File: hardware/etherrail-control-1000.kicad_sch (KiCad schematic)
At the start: 33 parts, among them J1 Conn_02x04_Odd_Even, J2 Conn_01x04, U1 AMS1117-3.3, U2 ESP32-C3, Y2 Crystal_GND24

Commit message: Fix missing crystal speed property
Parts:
- Y2: value Crystal_GND24 -> 16.000MHz GND24
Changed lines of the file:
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@@
       (effects (font (size 1.27 1.27)))
     )
-    (property "Value" "Crystal_GND24" (at 125.73 112.6491 0)
+    (property "Value" " 16.000MHz GND24" (at 125.73 112.6491 0)
       (effects (font (size 1.27 1.27)))
     )

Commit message: WIP: Add revised hardware
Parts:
- removed D5: D, Diode_SMD:D_SOD-323, symbol Device:D
- removed D8: Yellow, LED_SMD:LED_0603_1608Metric, symbol Device:LED
- added 3VR1: ME6118, Package_TO_SOT_SMD:SOT-89-3, symbol Regulator_Linear:AMS1117-3.3
- added C14: 1mF 6.3V, Capacitor_Tantalum_SMD:CP_EIA-7343-43_Kemet-X, symbol Device:C
- added D5: Yellow, LED_SMD:LED_0603_1608Metric, symbol Device:LED
- added JP1, JP2: Jumper_2_Open, Jumper:SolderJumper-2_P1.3mm_Open_Pad1.0x1.5mm, symbol Jumper:Jumper_2_Open
- added Q1, Q2: AO3400A, Package_TO_SOT_SMD:SOT-23, symbol Transistor_FET:AO3400A
- added R5: 100k, Resistor_SMD:R_0402_1005Metric, symbol Device:R
- added R6: 10k, Resistor_SMD:R_0201_0603Metric, symbol Device:R
- added R7: 22, Resistor_SMD:R_0201_0603Metric, symbol Device:R
- added R8: 5.1k, Resistor_SMD:R_0201_0603Metric, symbol Device:R
- 6VR1: renamed from U1; value AMS1117-3.3 -> 78N06G; LCSC (none) -> C84863
- C1: value 100uF -> 1mF 6.3V; footprint Capacitor_Tantalum_SMD:CP_EIA-7343-30_AVX-N -> Capacitor_Tantalum_SMD:CP_EIA-7343-43_Kemet-X; LCSC (none) -> C696799
- D7: LCSC (none) -> C19171392
- J2: footprint Connector_PinHeader_1.00mm:PinHeader_1x04_P1.00mm_Vertical -> Connector_PinHeader_1.27mm:PinHeader_1x04_P1.27mm_Vertical
- U2: LCSC (none) -> C2838500
- U3: LCSC (none) -> C2832995
- Y2: value 16.000MHz GND24 -> 40.000MHz 15pF; LCSC Part (none) -> C9010
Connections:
- net USB Power In is gone; now on net Light Common (+): J2.1 (Pin_1)
- net Unfiltered Power In is gone; now on net Light Common (+): D1.1 (K), D4.1 (K), D6.2 (A), R1.1, U3.4 (VDD)
- net Controller Power: now also 3VR1.2 (VO), R6.2, R8.1; no longer 6VR1.2 (VO)
- net GND: now also 3VR1.1 (GND), C14.2, D5.1 (K), JP1.2 (B), JP2.2 (B), Q1.2 (S), Q2.2 (S), R5.2
- net Light Front (-): now also Q1.3 (D)
- net Light Rear (-): now also Q2.3 (D)
- net Motor Controlling Direction: now also U2.24 (SPIQ/GPIO17); no longer U2.23 (SPID/GPIO16)
- net Motor Controlling PWM: now also U2.23 (SPID/GPIO16); no longer U2.24 (SPIQ/GPIO17)
- net USB Data Negative: now also J2.2 (Pin_2); no longer J2.3 (Pin_3)
- net USB Data Positive: now also J2.3 (Pin_3); no longer J2.2 (Pin_2)
- net at 6VR1.3 (VI), D6.1 (K): no longer C1.1
- net at C9.1, Y2.3: now also R7.1; no longer U2.30 (XTAL_P)
- net at R4.2: now also D5.2 (A)
- net at R4.1: now also U2.16 (GPIO10); no longer U2.14 (GPIO8)
- net Bootmode: now reaches U2.15 (GPIO9/BOOT)
- net Bootmode: now also JP1.1 (A), R8.2
- net Logic Level Light Front: now reaches U2.21 (SPICS0/GPIO14)
- net Logic Level Light Front: now also Q1.1 (G)
- net Logic Level Light Rear: now reaches U2.22 (SPICLK/GPIO15)
- net Logic Level Light Rear: now also Q2.1 (G)
- new net: 3VR1.3 (VI), 6VR1.2 (VO), C1.1, C14.1, R5.1
- new net: R7.2, U2.30 (XTAL_P)
- new net Download Enable: JP2.1 (A), R6.1, U2.14 (GPIO8)
- no-connect marks 19 -> 15
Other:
- moved on the sheet: 6VR1, C11, D7, J1, R1, R2, R3

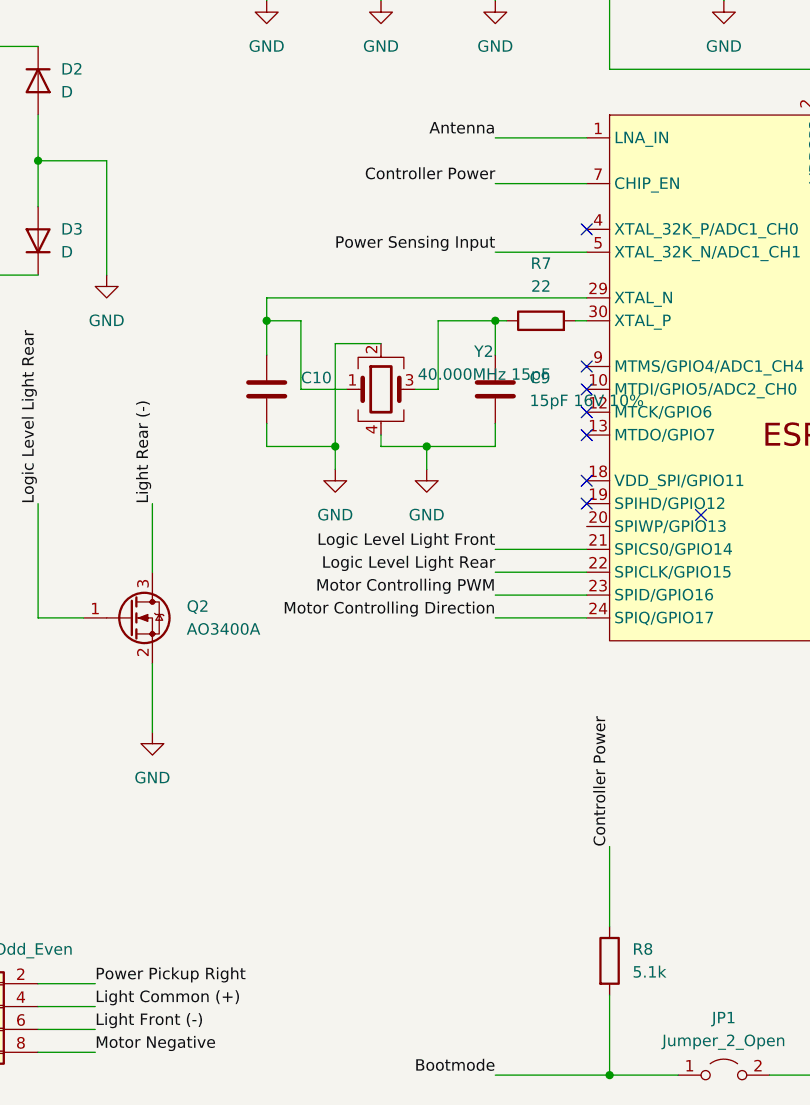
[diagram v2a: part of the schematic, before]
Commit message: Add EN jumper
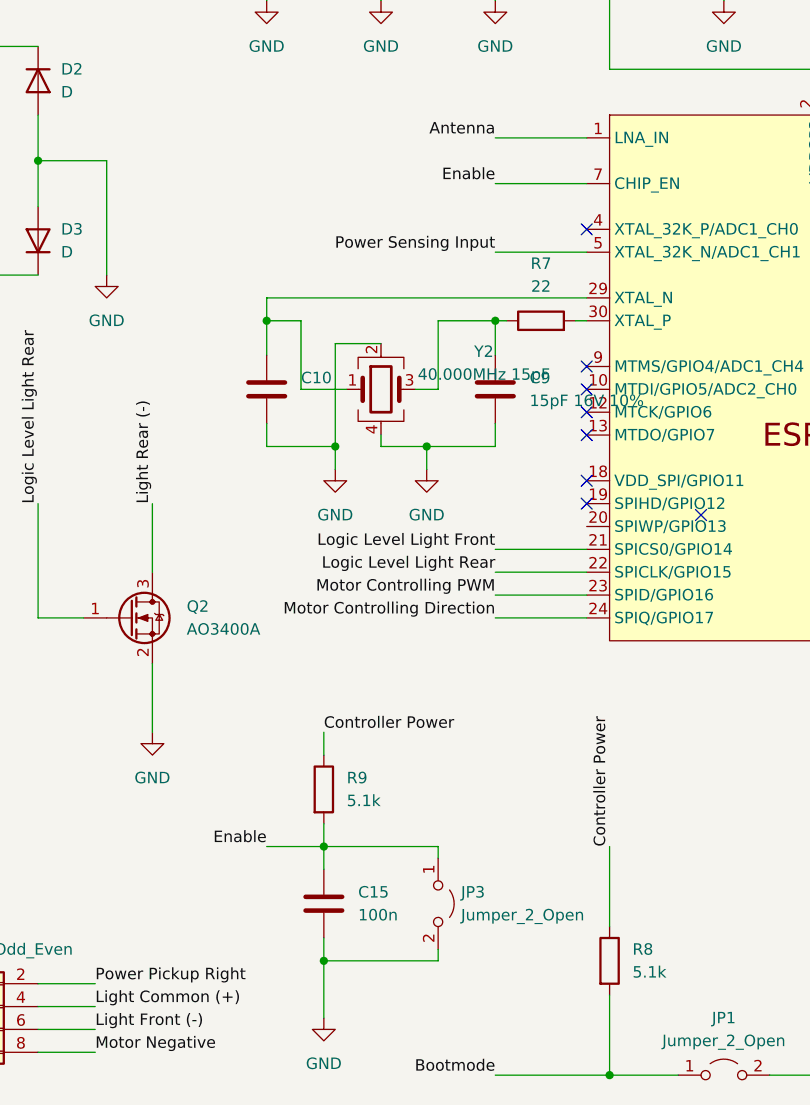
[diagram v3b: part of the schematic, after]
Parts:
- added C15: 100n, Capacitor_SMD:C_0201_0603Metric, symbol Device:C
- added JP3: Jumper_2_Open, Jumper:SolderJumper-2_P1.3mm_Open_Pad1.0x1.5mm, symbol Jumper:Jumper_2_Open
- added R9: 5.1k, Resistor_SMD:R_0201_0603Metric, symbol Device:R
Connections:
- net Controller Power: now also R9.1; no longer U2.7 (CHIP_EN)
- net GND: now also C15.2, JP3.2 (B)
- new net Enable: C15.1, JP3.1 (A), R9.2, U2.7 (CHIP_EN)
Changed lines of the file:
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@@
   (junction (at 127 106.68) (diameter 0) (color 0 0 0 0)
   )
+  (junction (at 107.95 165.1) (diameter 0) (color 0 0 0 0)
+  )
   (junction (at 203.2 57.15) (diameter 0) (color 0 0 0 0)
   )
@@
   )
   (junction (at 76.2 25.4) (diameter 0) (color 0 0 0 0)
+  )
+  (junction (at 107.95 177.8) (diameter 0) (color 0 0 0 0)
   )
   (junction (at 157.48 57.15) (diameter 0) (color 0 0 0 0)
@@
     (stroke (width 0) (type default))
   )
+  (wire (pts (xy 107.95 184.15) (xy 107.95 177.8))
+    (stroke (width 0) (type default))
+  )
   (wire (pts (xy 31.75 166.37) (xy 31.75 168.91))
     (stroke (width 0) (type default))
@@
     (stroke (width 0) (type default))
   )
+  (wire (pts (xy 107.95 165.1) (xy 107.95 162.56))
+    (stroke (width 0) (type default))
+  )
   (wire (pts (xy 57.15 187.96) (xy 63.5 187.96))
     (stroke (width 0) (type default))
@@
     (stroke (width 0) (type default))
   )
+  (wire (pts (xy 120.65 165.1) (xy 107.95 165.1))
+    (stroke (width 0) (type default))
+  )
   (wire (pts (xy 127 67.31) (xy 127 71.12))
     (stroke (width 0) (type default))
@@
     (stroke (width 0) (type default))
   )
+  (wire (pts (xy 107.95 165.1) (xy 107.95 167.64))
+    (stroke (width 0) (type default))
+  )
   (wire (pts (xy 88.9 25.4) (xy 88.9 34.29))
     (stroke (width 0) (type default))
@@
     (stroke (width 0) (type default))
   )
+  (wire (pts (xy 120.65 166.37) (xy 120.65 165.1))
+    (stroke (width 0) (type default))
+  )
   (wire (pts (xy 254 147.32) (xy 254 152.4))
     (stroke (width 0) (type default))
@@
     (stroke (width 0) (type default))
   )
+  (wire (pts (xy 107.95 177.8) (xy 120.65 177.8))
+    (stroke (width 0) (type default))
+  )
   (wire (pts (xy 38.1 38.1) (xy 38.1 25.4))
     (stroke (width 0) (type default))
@@
     (stroke (width 0) (type default))
   )
+  (wire (pts (xy 101.6 165.1) (xy 107.95 165.1))
+    (stroke (width 0) (type default))
+  )
   (wire (pts (xy 101.6 57.15) (xy 101.6 59.69))
     (stroke (width 0) (type default))
@@
     (stroke (width 0) (type default))
   )
+  (wire (pts (xy 107.95 152.4) (xy 107.95 154.94))
+    (stroke (width 0) (type default))
+  )
+  (wire (pts (xy 107.95 175.26) (xy 107.95 177.8))
+    (stroke (width 0) (type default))
+  )
   (wire (pts (xy 152.4 57.15) (xy 157.48 57.15))
     (stroke (width 0) (type default))
@@
     (stroke (width 0) (type default))
   )
+  (wire (pts (xy 120.65 176.53) (xy 120.65 177.8))
+    (stroke (width 0) (type default))
+  )
   (wire (pts (xy 237.49 44.45) (xy 228.6 44.45))
     (stroke (width 0) (type default))
@@
     (effects (font (size 1.27 1.27)) (justify right bottom))
   )
-  (label "Controller Power" (at 127 91.44 180) (fields_autoplaced)
-    (effects (font (size 1.27 1.27)) (justify right bottom))
-  )
   (label "Unfiltered Power In" (at 50.8 91.44 180) (fields_autoplaced)
     (effects (font (size 1.27 1.27)) (justify right bottom))
@@
     (effects (font (size 1.27 1.27)) (justify left bottom))
   )
+  (label "Enable" (at 101.6 165.1 180) (fields_autoplaced)
+    (effects (font (size 1.27 1.27)) (justify right bottom))
+  )
+  (label "Controller Power" (at 107.95 152.4 0) (fields_autoplaced)
+    (effects (font (size 1.27 1.27)) (justify left bottom))
+  )
   (label "Unfiltered Power In" (at 228.6 90.17 180) (fields_autoplaced)
     (effects (font (size 1.27 1.27)) (justify right bottom))
@@
   (label "Bootmode" (at 203.2 119.38 0) (fields_autoplaced)
     (effects (font (size 1.27 1.27)) (justify left bottom))
+  )
+  (label "Enable" (at 127 91.44 180) (fields_autoplaced)
+    (effects (font (size 1.27 1.27)) (justify right bottom))
   )
   (label "Logic Level Light Rear" (at 76.2 127 90) (fields_autoplaced)
@@
     )
   )
+  (symbol (lib_id "Jumper:Jumper_2_Open") (at 120.65 171.45 270) (unit 1)
+    (in_bom yes) (on_board yes) (dnp no) (fields_autoplaced)
+    (property "Reference" "JP3" (at 123.19 170.18 90)
+      (effects (font (size 1.27 1.27)) (justify left))
+    )
+    (property "Value" "Jumper_2_Open" (at 123.19 172.72 90)
+      (effects (font (size 1.27 1.27)) (justify left))
+    )
+    (property "Footprint" "Jumper:SolderJumper-2_P1.3mm_Open_Pad1.0x1.5mm" (at 120.65 171.45 0)
+      (effects (font (size 1.27 1.27)) hide)
+    )
+    (property "Datasheet" "~" (at 120.65 171.45 0)
+      (effects (font (size 1.27 1.27)) hide)
+    )
+    (pin "1")
+    (pin "2")
+    (instances
+      (project "etherrail-control-1000"
+        (path "/2c1a9b35-f6bb-4c65-94c1-f3bd4828dbaa"
+          (reference "JP3") (unit 1)
+        )
+      )
+    )
+  )
   (symbol (lib_id "Device:C") (at 76.2 38.1 0) (unit 1)
     (in_bom yes) (on_board yes) (dnp no) (fields_autoplaced)
@@
       (effects (font (size 1.27 1.27)) hide)
     )
-    (pin "2")
-    (pin "1")
+    (pin "1")
+    (pin "2")
     (instances
       (project "etherrail-control-1000"
@@
     )
   )
+  (symbol (lib_id "Device:R") (at 107.95 158.75 0) (unit 1)
+    (in_bom yes) (on_board yes) (dnp no) (fields_autoplaced)
+    (property "Reference" "R9" (at 110.49 157.48 0)
+      (effects (font (size 1.27 1.27)) (justify left))
+    )
+    (property "Value" "5.1k" (at 110.49 160.02 0)
+      (effects (font (size 1.27 1.27)) (justify left))
+    )
+    (property "Footprint" "Resistor_SMD:R_0201_0603Metric" (at 106.172 158.75 90)
+      (effects (font (size 1.27 1.27)) hide)
+    )
+    (property "Datasheet" "~" (at 107.95 158.75 0)
+      (effects (font (size 1.27 1.27)) hide)
+    )
+    (pin "1")
+    (pin "2")
+    (instances
+      (project "etherrail-control-1000"
+        (path "/2c1a9b35-f6bb-4c65-94c1-f3bd4828dbaa"
+          (reference "R9") (unit 1)
+        )
+      )
+    )
+  )
   (symbol (lib_id "Device:R") (at 132.08 106.68 90) (unit 1)
     (in_bom yes) (on_board yes) (dnp no) (fields_autoplaced)
@@
         (path "/2c1a9b35-f6bb-4c65-94c1-f3bd4828dbaa"
           (reference "R7") (unit 1)
+        )
+      )
+    )
+  )
+  (symbol (lib_id "Device:C") (at 107.95 171.45 0) (unit 1)
+    (in_bom yes) (on_board yes) (dnp no)
+    (property "Reference" "C15" (at 111.76 170.18 0)
+      (effects (font (size 1.27 1.27)) (justify left))
+    )
+    (property "Value" "100n" (at 111.76 172.72 0)
+      (effects (font (size 1.27 1.27)) (justify left))
+    )
+    (property "Footprint" "Capacitor_SMD:C_0201_0603Metric" (at 108.9152 175.26 0)
+      (effects (font (size 1.27 1.27)) hide)
+    )
+    (property "Datasheet" "~" (at 107.95 171.45 0)
+      (effects (font (size 1.27 1.27)) hide)
+    )
+    (pin "1")
+    (pin "2")
+    (instances
+      (project "etherrail-control-1000"
+        (path "/2c1a9b35-f6bb-4c65-94c1-f3bd4828dbaa"
+          (reference "C15") (unit 1)
         )
       )
@@
       (effects (font (size 1.27 1.27)) hide)
     )
-    (pin "2")
-    (pin "1")
+    (pin "1")
+    (pin "2")
     (instances
       (project "etherrail-control-1000"
@@
     )
   )
+  (symbol (lib_id "power:GND") (at 107.95 184.15 0) (unit 1)
+    (in_bom yes) (on_board yes) (dnp no) (fields_autoplaced)
+    (property "Reference" "#PWR021" (at 107.95 190.5 0)
+      (effects (font (size 1.27 1.27)) hide)
+    )
+    (property "Value" "GND" (at 107.95 189.23 0)
+      (effects (font (size 1.27 1.27)))
+    )
+    (property "Footprint" "" (at 107.95 184.15 0)
+      (effects (font (size 1.27 1.27)) hide)
+    )
+    (property "Datasheet" "" (at 107.95 184.15 0)
+      (effects (font (size 1.27 1.27)) hide)
+    )
+    (pin "1")
+    (instances
+      (project "etherrail-control-1000"
+        (path "/2c1a9b35-f6bb-4c65-94c1-f3bd4828dbaa"
+          (reference "#PWR021") (unit 1)
+        )
+      )
+    )
+  )
   (symbol (lib_id "Device:L") (at 241.3 133.35 90) (unit 1)
     (in_bom yes) (on_board yes) (dnp no) (fields_autoplaced)
@@
       (effects (font (size 1.27 1.27)) hide)
     )
-    (pin "2")
-    (pin "1")
-    (instances
-      (project "etherrail-control-1000"
+    (pin "1")
+    (pin "2")
+    (instances
+      (project "etherrail-control-1000"

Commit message: Add GPIO2 rotue
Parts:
- added R10: 5.1k, Resistor_SMD:R_0201_0603Metric, symbol Device:R
- R6: value 10k -> 5.1k
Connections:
- net Controller Power: now also R10.2
- net at U2.6 (GPIO2/ADC1_CH2): now also R10.1
- no-connect marks 15 -> 14
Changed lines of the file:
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@@
   (no_connect (at 193.04 114.3))
   (no_connect (at 137.16 114.3))
-  (no_connect (at 193.04 111.76))
   (no_connect (at 234.95 100.33))
   (no_connect (at 137.16 111.76))
@@
     (stroke (width 0) (type default))
   )
+  (wire (pts (xy 193.04 111.76) (xy 199.39 111.76))
+    (stroke (width 0) (type default))
+  )
+  (wire (pts (xy 207.01 111.76) (xy 215.9 111.76))
+    (stroke (width 0) (type default))
+  )
   (wire (pts (xy 127 57.15) (xy 127 59.69))
     (stroke (width 0) (type default))
@@
   )
   (label "Controller Power" (at 203.2 50.8 0) (fields_autoplaced)
+    (effects (font (size 1.27 1.27)) (justify left bottom))
+  )
+  (label "Controller Power" (at 215.9 111.76 0) (fields_autoplaced)
     (effects (font (size 1.27 1.27)) (justify left bottom))
   )
@@
       (effects (font (size 1.27 1.27)))
     )
-    (property "Value" "10k" (at 241.3 40.64 90)
+    (property "Value" "5.1k" (at 241.3 40.64 90)
       (effects (font (size 1.27 1.27)))
     )
@@
         )
       )
+    )
+  )
+  (symbol (lib_id "Device:R") (at 203.2 111.76 90) (unit 1)
+    (in_bom yes) (on_board yes) (dnp no) (fields_autoplaced)
+    (property "Reference" "R10" (at 203.2 105.41 90)
+      (effects (font (size 1.27 1.27)))
+    )
+    (property "Value" "5.1k" (at 203.2 107.95 90)
+      (effects (font (size 1.27 1.27)))
+    )
+    (property "Footprint" "Resistor_SMD:R_0201_0603Metric" (at 203.2 113.538 90)
+      (effects (font (size 1.27 1.27)) hide)
+    )
+    (property "Datasheet" "~" (at 203.2 111.76 0)
+      (effects (font (size 1.27 1.27)) hide)
+    )
+    (pin "1")
+    (pin "2")
+    (instances
+      (project "etherrail-control-1000"
+        (path "/2c1a9b35-f6bb-4c65-94c1-f3bd4828dbaa"
+          (reference "R10") (unit 1)
+        )
+      )

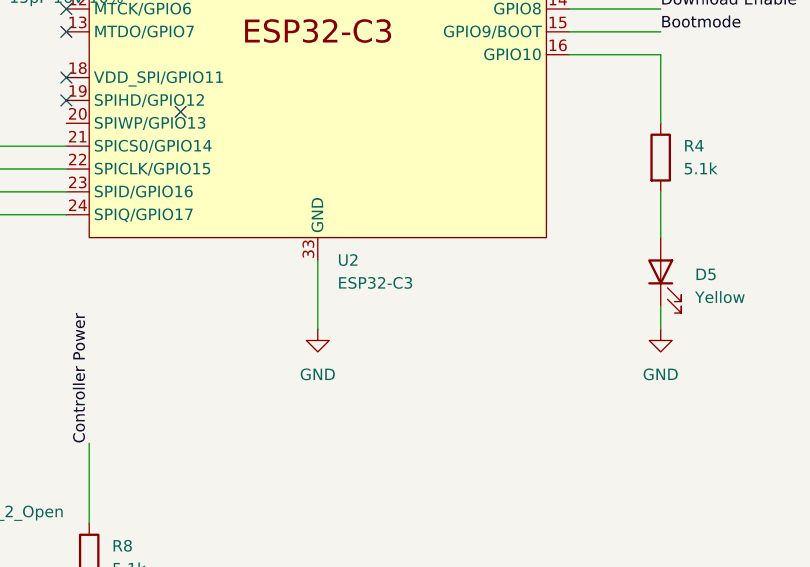
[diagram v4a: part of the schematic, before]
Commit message: Fix use ESP32-C3 with flash (C3-FH4)
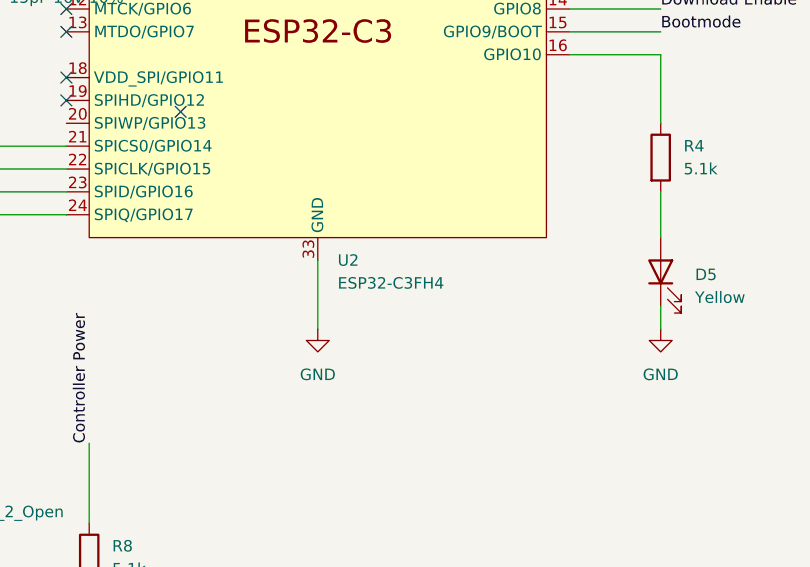
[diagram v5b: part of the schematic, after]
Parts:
- U2: value ESP32-C3 -> ESP32-C3FH4; footprint Package_DFN_QFN:QFN-32-1EP_5x5mm_P0.5mm_EP3.45x3.45mm -> Package_DFN_QFN:QFN-32-1EP_5x5mm_P0.5mm_EP3.1x3.1mm; LCSC C2838500 -> C2858491
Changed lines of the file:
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@@
       (effects (font (size 1.27 1.27)) (justify left))
     )
-    (property "Value" "ESP32-C3" (at 167.2941 147.32 0)
+    (property "Value" "ESP32-C3FH4" (at 167.2941 147.32 0)
       (effects (font (size 1.27 1.27)) (justify left))
     )
-    (property "Footprint" "Package_DFN_QFN:QFN-32-1EP_5x5mm_P0.5mm_EP3.45x3.45mm" (at 165.1 152.4 0)
+    (property "Footprint" "Package_DFN_QFN:QFN-32-1EP_5x5mm_P0.5mm_EP3.1x3.1mm" (at 165.1 152.4 0)
       (effects (font (size 1.27 1.27)) hide)
     )
@@
       (effects (font (size 1.27 1.27)) hide)
     )
-    (property "LCSC" "C2838500" (at 165.1 114.3 0)
+    (property "LCSC" "C2858491" (at 165.1 114.3 0)
       (effects (font (size 1.27 1.27)) hide)
     )
